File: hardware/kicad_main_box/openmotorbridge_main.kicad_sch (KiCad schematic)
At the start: 0 parts

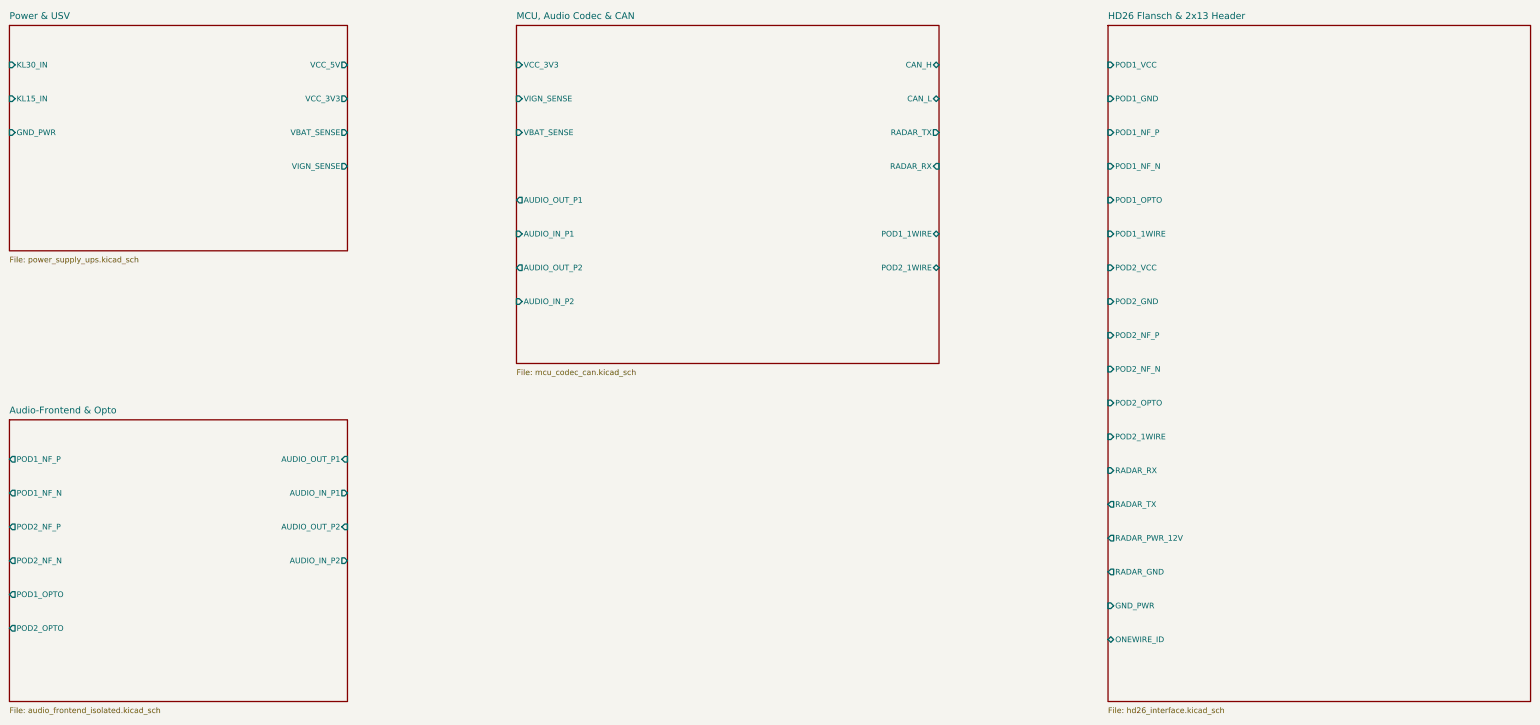
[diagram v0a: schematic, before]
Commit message: hardware(main-box): remove legacy audio isolation barrier and obsolete sheets
- remove 4mm silkscreen isolation line and barrier text annotations
- merge split internal audio zone on In1.Cu to unified GND_PWR plane
- remove obsolete DNP Audio-Frontend & Opto sheet from top-level schematic
- update top-level schematic interface sheet to Deutsch DTM-12
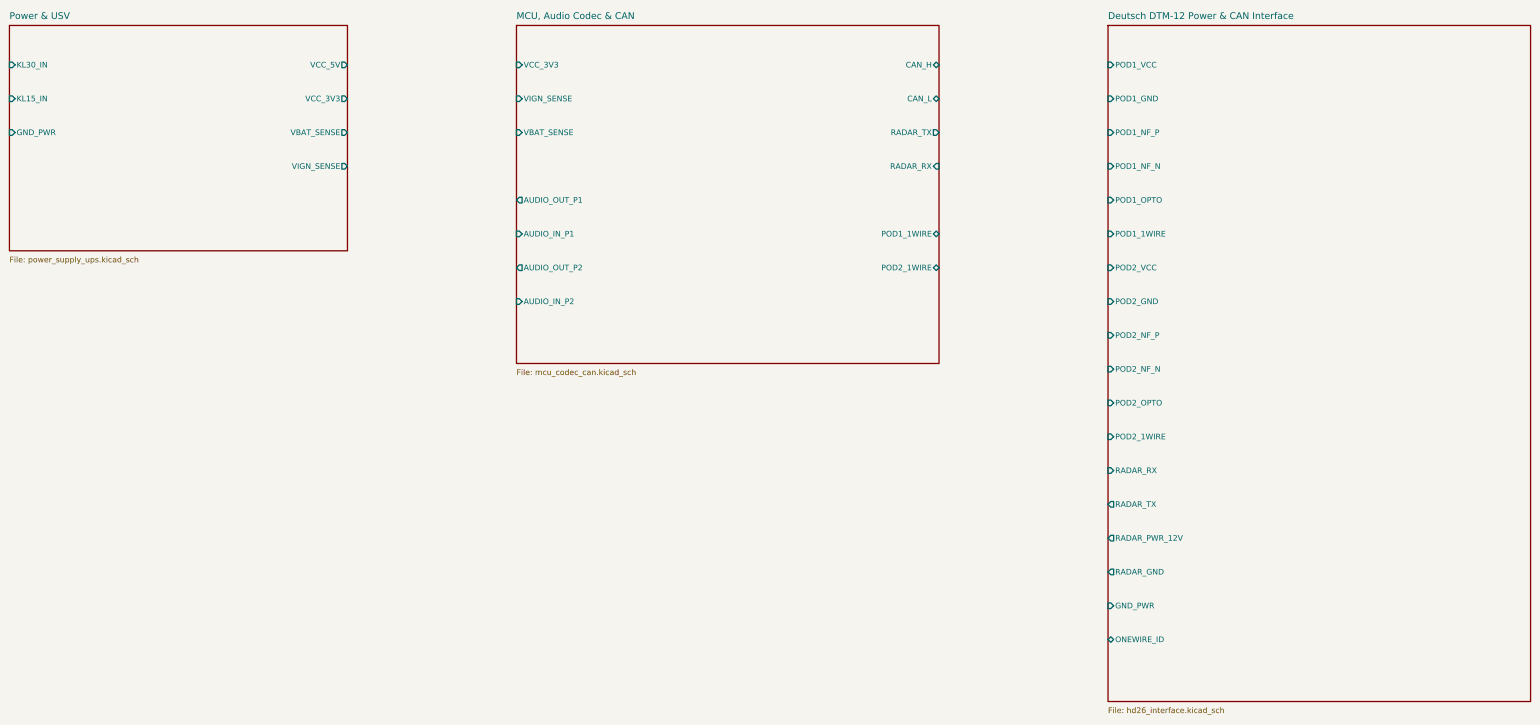
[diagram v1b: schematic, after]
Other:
- sheet HD26 Flansch & 2x13 Header renamed Deutsch DTM-12 Power & CAN Interface
- removed sheet Audio-Frontend & Opto
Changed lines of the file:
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@@
 		(company "OpenMotorBridge Open Source Hardware")
 		(comment 1 "Universelles 4-Punkte-Satelliten-Gateway (CERN-OHL-S v2)")
-		(comment 2 "HD26 26-Pin Matrix, ES8388 24-Bit Codec, TCAN334G CAN-FD")
+		(comment 2 "Deutsch DTM-12 Automotive Matrix, ES8388 DSP Codec, TCAN334G CAN-FD, Qorvo DW3110 UWB")
 	)
 	(sheet
@@
 	)
 	(sheet
-		(at 38.1 133.35)
-		(size 76.2 63.5)
-		(exclude_from_sim yes)
-		(in_bom no)
-		(on_board no)
-		(dnp yes)
-		(stroke
-			(width 0.254)
-			(type solid)
-		)
-		(fill
-			(color 22 27 34 0.8)
-		)
-		(property "Sheetname" "Audio-Frontend & Opto"
-			(at 38.1 132.08 0)
-			(show_name no)
-			(do_not_autoplace no)
-			(effects
-				(font
-					(size 1.524 1.524)
-				)
-				(justify left bottom)
-			)
-		)
-		(property "Sheetfile" "audio_frontend_isolated.kicad_sch"
-			(at 38.1 198.12 0)
-			(show_name no)
-			(do_not_autoplace no)
-			(effects
-				(font
-					(size 1.27 1.27)
-				)
-				(justify left top)
-			)
-		)
-		(pin "AUDIO_OUT_P1" input
-			(at 114.3 142.24 0)
-			(effects
-				(font
-					(size 1.27 1.27)
-				)
-				(justify right)
-			)
-		)
-		(pin "AUDIO_IN_P1" output
-			(at 114.3 149.86 0)
-			(effects
-				(font
-					(size 1.27 1.27)
-				)
-				(justify right)
-			)
-		)
-		(pin "AUDIO_OUT_P2" input
-			(at 114.3 157.48 0)
-			(effects
-				(font
-					(size 1.27 1.27)
-				)
-				(justify right)
-			)
-		)
-		(pin "AUDIO_IN_P2" output
-			(at 114.3 165.1 0)
-			(effects
-				(font
-					(size 1.27 1.27)
-				)
-				(justify right)
-			)
-		)
-		(pin "POD1_NF_P" output
-			(at 38.1 142.24 180)
-			(effects
-				(font
-					(size 1.27 1.27)
-				)
-				(justify left)
-			)
-		)
-		(pin "POD1_NF_N" output
-			(at 38.1 149.86 180)
-			(effects
-				(font
-					(size 1.27 1.27)
-				)
-				(justify left)
-			)
-		)
-		(pin "POD2_NF_P" output
-			(at 38.1 157.48 180)
-			(effects
-				(font
-					(size 1.27 1.27)
-				)
-				(justify left)
-			)
-		)
-		(pin "POD2_NF_N" output
-			(at 38.1 165.1 180)
-			(effects
-				(font
-					(size 1.27 1.27)
-				)
-				(justify left)
-			)
-		)
-		(pin "POD1_OPTO" output
-			(at 38.1 172.72 180)
-			(effects
-				(font
-					(size 1.27 1.27)
-				)
-				(justify left)
-			)
-		)
-		(pin "POD2_OPTO" output
-			(at 38.1 180.34 180)
-			(effects
-				(font
-					(size 1.27 1.27)
-				)
-				(justify left)
-			)
-		)
-		(instances
-			(project "openmotorbridge_main"
-				(path "/a0000000-0000-0000-0000-000000000001"
-					(page "3")
-				)
-			)
-		)
-	)
-	(sheet
 		(at 285.75 44.45)
 		(size 95.25 152.4)
@@
 			(color 22 27 34 0.8)
 		)
-		(property "Sheetname" "HD26 Flansch & 2x13 Header"
+		(property "Sheetname" "Deutsch DTM-12 Power & CAN Interface"
 			(at 285.75 43.18 0)
 			(show_name no)

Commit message: hardware(cartridge): move ES8388 audio codec to B.Cu bottom layer to eliminate overlaps and isolate from actuator MOSFETs
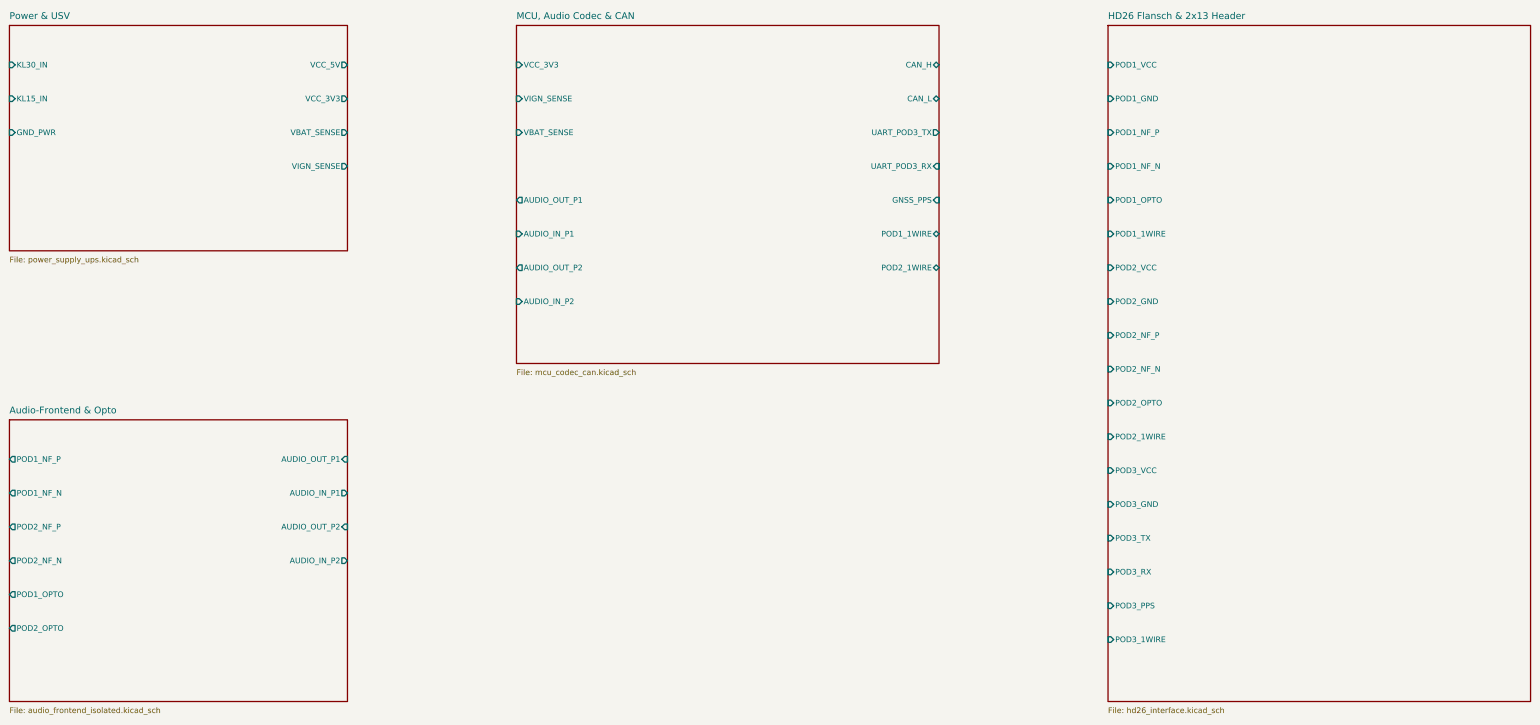
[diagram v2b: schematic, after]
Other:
- sheet Deutsch DTM-12 Power & CAN Interface renamed HD26 Flansch & 2x13 Header
- added sheet Audio-Frontend & Opto (audio_frontend_isolated.kicad_sch)
- sheet HD26 Flansch & 2x13 Header ports: added POD3_1WIRE, POD3_GND, POD3_PPS, POD3_RX, POD3_TX, POD3_VCC; removed GND_PWR, ONEWIRE_ID, RADAR_GND, RADAR_PWR_12V, RADAR_RX, RADAR_TX
- sheet MCU, Audio Codec & CAN ports: added GNSS_PPS, UART_POD3_RX, UART_POD3_TX; removed RADAR_RX, RADAR_TX
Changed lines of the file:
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@@
 		(company "OpenMotorBridge Open Source Hardware")
 		(comment 1 "Universelles 4-Punkte-Satelliten-Gateway (CERN-OHL-S v2)")
-		(comment 2 "Deutsch DTM-12 Automotive Matrix, ES8388 DSP Codec, TCAN334G CAN-FD, Qorvo DW3110 UWB")
+		(comment 2 "HD26 26-Pin Matrix, ES8388 24-Bit Codec, TCAN334G CAN-FD")
 	)
 	(sheet
@@
 			)
 		)
-		(pin "RADAR_TX" output
+		(pin "UART_POD3_TX" output
 			(at 247.65 68.58 0)
 			(effects
@@
 			)
 		)
-		(pin "RADAR_RX" input
+		(pin "UART_POD3_RX" input
 			(at 247.65 76.2 0)
+			(effects
+				(font
+					(size 1.27 1.27)
+				)
+				(justify right)
+			)
+		)
+		(pin "GNSS_PPS" input
+			(at 247.65 83.82 0)
 			(effects
 				(font
@@
 				(path "/a0000000-0000-0000-0000-000000000001"
 					(page "4")
+				)
+			)
+		)
+	)
+	(sheet
+		(at 38.1 133.35)
+		(size 76.2 63.5)
+		(exclude_from_sim no)
+		(in_bom yes)
+		(on_board yes)
+		(dnp no)
+		(stroke
+			(width 0.254)
+			(type solid)
+		)
+		(fill
+			(color 22 27 34 0.8)
+		)
+		(property "Sheetname" "Audio-Frontend & Opto"
+			(at 38.1 132.08 0)
+			(show_name no)
+			(do_not_autoplace no)
+			(effects
+				(font
+					(size 1.524 1.524)
+				)
+				(justify left bottom)
+			)
+		)
+		(property "Sheetfile" "audio_frontend_isolated.kicad_sch"
+			(at 38.1 198.12 0)
+			(show_name no)
+			(do_not_autoplace no)
+			(effects
+				(font
+					(size 1.27 1.27)
+				)
+				(justify left top)
+			)
+		)
+		(pin "AUDIO_OUT_P1" input
+			(at 114.3 142.24 0)
+			(effects
+				(font
+					(size 1.27 1.27)
+				)
+				(justify right)
+			)
+		)
+		(pin "AUDIO_IN_P1" output
+			(at 114.3 149.86 0)
+			(effects
+				(font
+					(size 1.27 1.27)
+				)
+				(justify right)
+			)
+		)
+		(pin "AUDIO_OUT_P2" input
+			(at 114.3 157.48 0)
+			(effects
+				(font
+					(size 1.27 1.27)
+				)
+				(justify right)
+			)
+		)
+		(pin "AUDIO_IN_P2" output
+			(at 114.3 165.1 0)
+			(effects
+				(font
+					(size 1.27 1.27)
+				)
+				(justify right)
+			)
+		)
+		(pin "POD1_NF_P" output
+			(at 38.1 142.24 180)
+			(effects
+				(font
+					(size 1.27 1.27)
+				)
+				(justify left)
+			)
+		)
+		(pin "POD1_NF_N" output
+			(at 38.1 149.86 180)
+			(effects
+				(font
+					(size 1.27 1.27)
+				)
+				(justify left)
+			)
+		)
+		(pin "POD2_NF_P" output
+			(at 38.1 157.48 180)
+			(effects
+				(font
+					(size 1.27 1.27)
+				)
+				(justify left)
+			)
+		)
+		(pin "POD2_NF_N" output
+			(at 38.1 165.1 180)
+			(effects
+				(font
+					(size 1.27 1.27)
+				)
+				(justify left)
+			)
+		)
+		(pin "POD1_OPTO" output
+			(at 38.1 172.72 180)
+			(effects
+				(font
+					(size 1.27 1.27)
+				)
+				(justify left)
+			)
+		)
+		(pin "POD2_OPTO" output
+			(at 38.1 180.34 180)
+			(effects
+				(font
+					(size 1.27 1.27)
+				)
+				(justify left)
+			)
+		)
+		(instances
+			(project "openmotorbridge_main"
+				(path "/a0000000-0000-0000-0000-000000000001"
+					(page "3")
 				)
 			)
@@
 			(color 22 27 34 0.8)
 		)
-		(property "Sheetname" "Deutsch DTM-12 Power & CAN Interface"
+		(property "Sheetname" "HD26 Flansch & 2x13 Header"
 			(at 285.75 43.18 0)
 			(show_name no)
@@
 			)
 		)
-		(pin "RADAR_RX" input
+		(pin "POD3_VCC" input
 			(at 285.75 144.78 180)
 			(effects
@@
 			)
 		)
-		(pin "RADAR_TX" output
+		(pin "POD3_GND" input
 			(at 285.75 152.4 180)
 			(effects
@@
 			)
 		)
-		(pin "RADAR_PWR_12V" output
+		(pin "POD3_TX" input
 			(at 285.75 160.02 180)
 			(effects
@@
 			)
 		)
-		(pin "RADAR_GND" output
+		(pin "POD3_RX" input
 			(at 285.75 167.64 180)
 			(effects
@@
 			)
 		)
-		(pin "GND_PWR" input
+		(pin "POD3_PPS" input
 			(at 285.75 175.26 180)
 			(effects
@@
 			)
 		)
-		(pin "ONEWIRE_ID" bidirectional
+		(pin "POD3_1WIRE" input
 			(at 285.75 182.88 180)
 			(effects

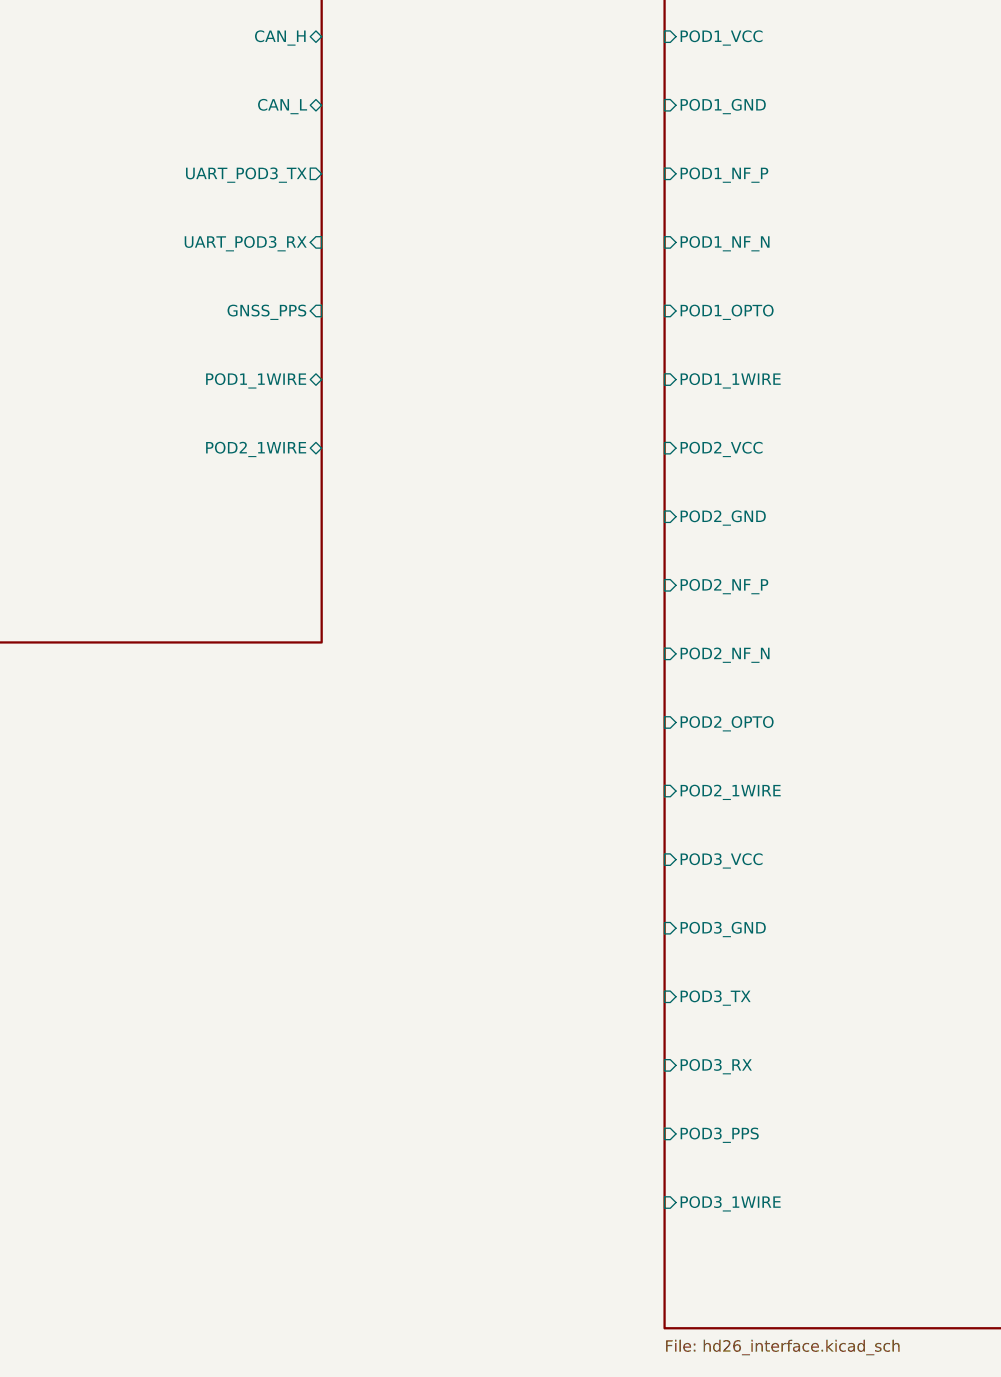
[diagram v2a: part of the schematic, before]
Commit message: feat(arch): finalize v8.5/v9.0 Clean All-UWB Architecture, 6-PCBA lineup and Pure-DC wiring in documentation
- All-UWB Interconnects: Central Box communicates with Front-Node, Bay 1 (Left), Bay 2 (Right), and Rear Radar strictly over Qorvo DW3110 UWB (6.489 GHz Ch. 5, <0.4 ms latency, AES-128-CCM).
- Symmetrical Mounting Bays: Pod 1 and Pod 2 are physical docking bays (Bucht 1 / Bucht 2, Left / Right) for gateway units, NOT Fahrer / Sozius. Rider and pillion helmets connect directly via Bluetooth to Central Box DSP.
- 6-PCBA Lineup: PCBA 02 (Pod Base) and PCBA 04 (Rear Pod 3) retired and archived. Pod enclosures use direct 2-wire DC leaf spring contacts (+5V/GND). PCBA 03 is 2-sided SMT with DW3110, Host-MCU, and 4x AO3400A MOSFETs.
- Deutsch DTM-12 Harness: Replaced HD26 connector with 12-pin Deutsch DTM-12 automotive connector providing pure DC power.
- Power Sequencing & Roaming: Boot sequence (T=0, 200, 350, 500 ms), HW button SW1 (pairing & NVS reset), and 4-vehicle NVS roaming.
- Documentation Updated: docs/de/ 01, 03, 04, 07, 08, 09, 13, 14, 15, 16, status.md, DECISIONS_LOG.md (ADR-011), and hardware/README.md.
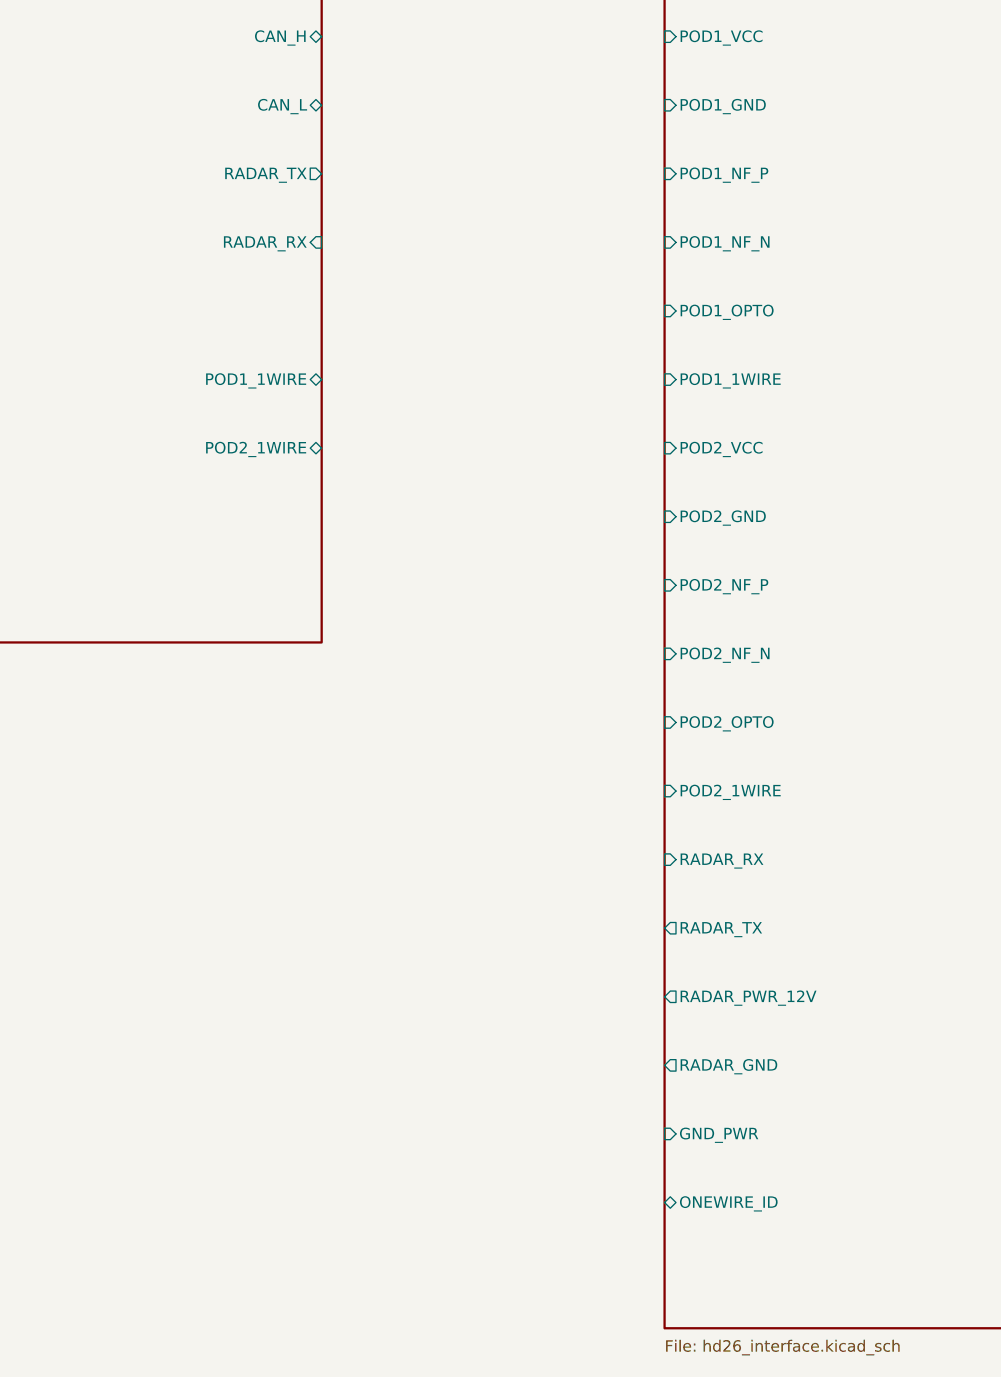
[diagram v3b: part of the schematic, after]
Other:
- sheet HD26 Flansch & 2x13 Header ports: added GND_PWR, ONEWIRE_ID, RADAR_GND, RADAR_PWR_12V, RADAR_RX, RADAR_TX; removed POD3_1WIRE, POD3_GND, POD3_PPS, POD3_RX, POD3_TX, POD3_VCC
- sheet MCU, Audio Codec & CAN ports: added RADAR_RX, RADAR_TX; removed GNSS_PPS, UART_POD3_RX, UART_POD3_TX
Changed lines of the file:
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@@
 			)
 		)
-		(pin "UART_POD3_TX" output
+		(pin "RADAR_TX" output
 			(at 247.65 68.58 0)
 			(effects
@@
 			)
 		)
-		(pin "UART_POD3_RX" input
+		(pin "RADAR_RX" input
 			(at 247.65 76.2 0)
-			(effects
-				(font
-					(size 1.27 1.27)
-				)
-				(justify right)
-			)
-		)
-		(pin "GNSS_PPS" input
-			(at 247.65 83.82 0)
 			(effects
 				(font
@@
 		(at 38.1 133.35)
 		(size 76.2 63.5)
-		(exclude_from_sim no)
-		(in_bom yes)
-		(on_board yes)
-		(dnp no)
+		(exclude_from_sim yes)
+		(in_bom no)
+		(on_board no)
+		(dnp yes)
 		(stroke
 			(width 0.254)
@@
 			)
 		)
-		(pin "POD3_VCC" input
+		(pin "RADAR_RX" input
 			(at 285.75 144.78 180)
 			(effects
@@
 			)
 		)
-		(pin "POD3_GND" input
+		(pin "RADAR_TX" output
 			(at 285.75 152.4 180)
 			(effects
@@
 			)
 		)
-		(pin "POD3_TX" input
+		(pin "RADAR_PWR_12V" output
 			(at 285.75 160.02 180)
 			(effects
@@
 			)
 		)
-		(pin "POD3_RX" input
+		(pin "RADAR_GND" output
 			(at 285.75 167.64 180)
 			(effects
@@
 			)
 		)
-		(pin "POD3_PPS" input
+		(pin "GND_PWR" input
 			(at 285.75 175.26 180)
 			(effects
@@
 			)
 		)
-		(pin "POD3_1WIRE" input
+		(pin "ONEWIRE_ID" bidirectional
 			(at 285.75 182.88 180)
 			(effects
